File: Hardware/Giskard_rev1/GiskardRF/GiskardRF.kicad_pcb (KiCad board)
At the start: 4 copper layers, 79.8 x 43.7 mm, 68 parts, among them J101 USB_B_Micro, J102 Conn_ARM_JTAG_SWD_20, J103 Test pins COMM2, J104 Test pins COMM1, J201 SMA6252A23G50, J305 Conn_01x16, J306 Conn_01x16, SW101 RESET, U101 USBLC6-2P6, U102 FT230XQ, U103 AP22802AW5-7, U104 AP2127K-3.3, U105 M24C16-RM, U106 STM32G070CBTx, U107 APX823, U201 RFM69HW, U303 AP22802AW5-7, Y101 3225-16M-SR 16MHz 9pF, Y102 32.768K-CFPX217

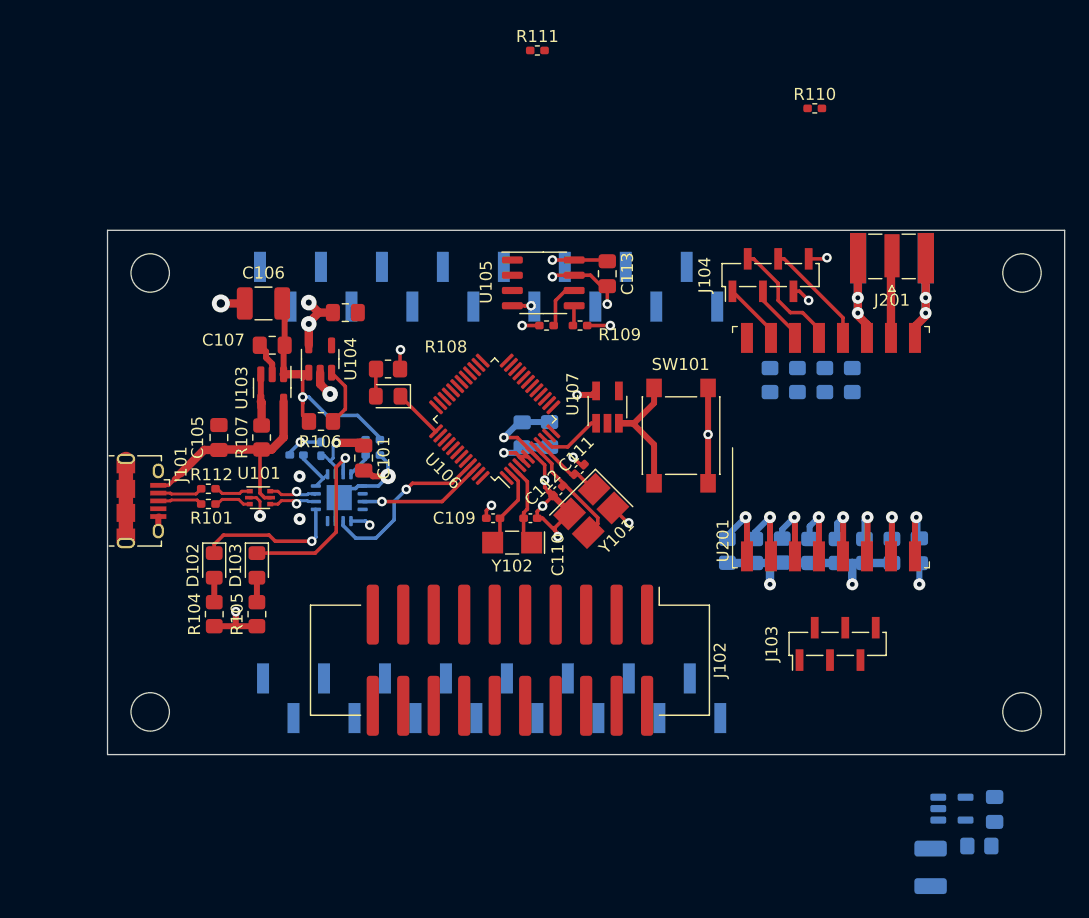
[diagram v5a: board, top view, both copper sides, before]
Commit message: Finished Giskard layout
- Need to fix DRC violations
- It'd be nice to move EEPROM closer to MPU
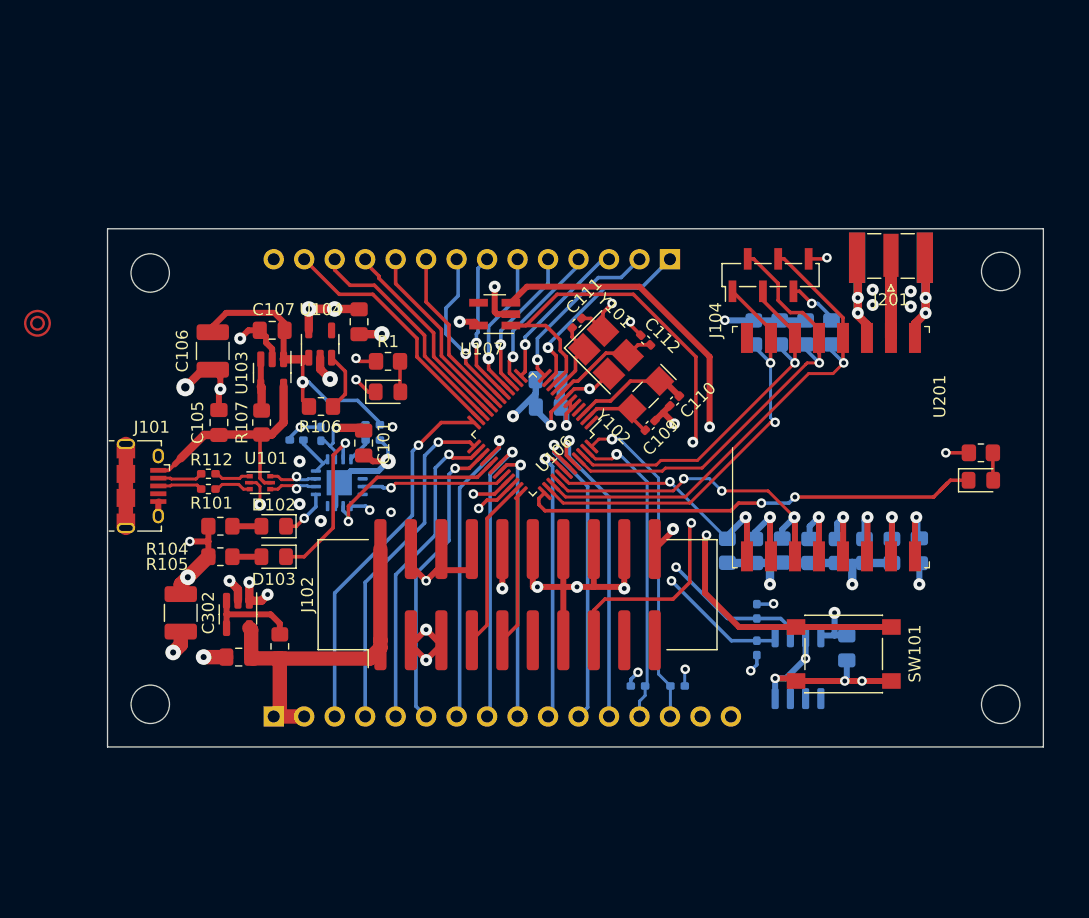
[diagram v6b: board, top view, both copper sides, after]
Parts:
- removed J103: Test pins COMM2, Connector_PinSocket_1.27mm:PinSocket_1x06_P1.27mm_Vertical_SMD_Pin1Left
- added D1: PWR_LED, Diode_SMD:D_0805_2012Metric_Pad1.15x1.40mm_HandSolder, F.Cu at (135.9, 109.5)
- added R1: 330, Resistor_SMD:R_0805_2012Metric_Pad1.20x1.40mm_HandSolder, F.Cu at (135.9, 106.9)
- C113, R108, R109, R110, R111, U105: moved to B.Cu
- C301, C302, R301, U303: moved to F.Cu
- J305: value Conn_01x16 -> Conn_01x14; footprint Connector_PinHeader_2.54mm:PinHeader_1x16_P2.54mm_Vertical_SMD_Pin1Left -> Connector_PinHeader_2.54mm:PinHeader_1x14_P2.54mm_Vertical
- J306: footprint Connector_PinHeader_2.54mm:PinHeader_1x16_P2.54mm_Vertical_SMD_Pin1Left -> Connector_PinHeader_2.54mm:PinHeader_1x16_P2.54mm_Vertical
- R102, R104, R105: value 270 -> 330
- moved C302 66.0 mm to (118.6, 127.9), turned to -90 degrees
- moved C301 64.3 mm to (123.4, 131.6), turned to 180 degrees
- moved U303 61.7 mm to (123.4, 128.0), turned to -90 degrees
- moved R301 60.6 mm to (126.9, 130.7), turned to 90 degrees
- moved R111 54.2 mm to (160.0, 134.0), turned to 180 degrees
- moved R110 50.3 mm to (156.7, 134.0)
- moved R102 49.9 mm to (185.3, 114.6), turned to 0 degrees
- moved D101 49.9 mm to (185.3, 116.8), turned to 0 degrees
- moved U105 38.5 mm to (170.1, 132.5), turned to 90 degrees
- moved C113 37.0 mm to (174.1, 130.8)
- moved R109 30.6 mm to (166.6, 130.8), turned to 90 degrees
- moved R108 29.6 mm to (166.6, 127.8), turned to -90 degrees
- moved SW101 22.7 mm to (173.9, 131.3), turned to 180 degrees
- moved J306 18.2 mm to (126.4, 136.5)
- moved Y102 16.6 mm to (157.4, 109.7), turned to -135 degrees
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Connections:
- J305 pad 1: GNDD -> /GPIO_PA0
- J305 pad 10: /GPIO_PA0 -> /GPIO_PB1
- J305 pad 11: /GPIO_PA8 -> /GPIO_PB2
- J305 pad 12: /GPIO_PB15 -> /GPIO_PB10
- J305 pad 13: /GPIO_PB14 -> /GPIO_PB11
- J305 pad 14: /GPIO_PB13 -> GNDD
- J305 pad 2: GNDD -> /GPIO_PA1
- J305 pad 3: /GPIO_PA3 -> /GPIO_PA2
- J305 pad 4: /GPIO_PA4 -> /GPIO_PA3
- J305 pad 5: /SPI1_SCK -> /GPIO_PA4
- J305 pad 6: /SPI1_MISO -> /SPI1_SCK
- J305 pad 7: /SPI1_MOSI -> /SPI1_MISO
- J305 pad 8: /GPIO_PA2 -> /SPI1_MOSI
- J305 pad 9: /GPIO_PA1 -> /GPIO_PB0
- J306 pad 11: /GPIO_PC13 -> /GPIO_PB4
- J306 pad 12: /GPIO_PB9 -> /GPIO_PB5
- J306 pad 13: /GPIO_PB8 -> /I2C1_SCL
- J306 pad 14: /GPIO_PB4 -> /I2C1_SDA
- J306 pad 2: /GPIO_PD0 -> /CON_PWR
- J306 pad 3: /GPIO_PD1 -> /GPIO_PB12
- J306 pad 4: /GPIO_PD2 -> /GPIO_PB13
- J306 pad 5: /GPIO_PC7 -> /GPIO_PB14
- J306 pad 6: /GPIO_PC6 -> /GPIO_PB15
- J306 pad 7: /I2C1_SCL -> /GPIO_PA8
- J306 pad 8: /I2C1_SDA -> /GPIO_PC6
- J306 pad 9: /GPIO_PD3 -> /GPIO_PC7
- U106 pad 19: /RF_RESET -> /GPIO_PB0
- U106 pad 20: /RF_FIFO_F_NE -> /GPIO_PB1
- U106 pad 21: /SPI2_MISO -> /GPIO_PB2
- U106 pad 22: /SPI2_SCK -> /GPIO_PB10
- U106 pad 23: /SPI2_MOSI -> /GPIO_PB11
- U106 pad 24: /SPI2_NSS -> /GPIO_PB12
- U106 pad 29: /I2C1_SCL -> /USART1_TX
- U106 pad 32: /I2C1_SDA -> /USART1_RX
- U106 pad 38: /GPIO_PD0 -> /SPI2_NSS
- U106 pad 39: /GPIO_PD1 -> /SPI2_SCK
- U106 pad 40: /GPIO_PD2 -> /RF_FIFO_F_NE
- U106 pad 41: /GPIO_PD3 -> /RF_RESET
- U106 pad 45: /USART1_TX -> /SPI2_MISO
- U106 pad 46: /USART1_RX -> /SPI2_MOSI
- U106 pad 47: /GPIO_PB8 -> /I2C1_SCL
- U106 pad 48: /GPIO_PB9 -> /I2C1_SDA
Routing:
- net GNDD: track 117.3 -> 190.3 mm, vias 27 -> 49
- net /~{RESET}: track 5.33 -> 58.6 mm, vias 0 -> 2
- net Net-(SW101-A): track 11.8 -> 56.1 mm, vias 0 -> 2
- net /~{ERR_LED}: track 4.29 -> 39.5 mm, vias 0 -> 2
- net /I2C2_SCL_MEM: track 1.70 -> 36.4 mm, vias 0 -> 2
- net /SPI2_SCK: track 9.12 -> 42.4 mm, vias 0 -> 1
- net /SPI2_NSS: track 5.22 -> 36.7 mm, vias 0 -> 2
- net /GPIO_PB12: track 0.00 -> 30.9 mm, vias 0 -> 1
- net /I2C2_SDA_MEM: track 4.05 -> 34.9 mm, vias 0 -> 2
- net /CON_PWR: track 0.00 -> 29.5 mm
- net /GPIO_PB13: track 0.00 -> 28.5 mm, vias 0 -> 1
- net /SPI2_MISO: track 9.93 -> 38.2 mm, vias 0 -> 1
- net /I2C1_SDA: track 0.00 -> 27.5 mm, vias 0 -> 1
- net /GPIO_PB5: track 0.00 -> 26.6 mm, vias 0 -> 1
- net /GPIO_PB4: track 0.00 -> 26.5 mm, vias 0 -> 1
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- added copper zone on In2.Cu, net +3V3
- added copper zone on In1.Cu, net GNDD
- added copper zone on In2.Cu, net GNDD
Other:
- board size 79.8 x 43.7 mm -> 78 x 43.2 mm

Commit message: Finished board layout
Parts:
- D101: value ERR_LED (RED) -> ERR_LED
- moved D1 49.4 mm to (185.2, 112.8)
- moved R1 49.4 mm to (185.2, 110.2)
- moved C113 22.7 mm to (152.0, 125.6)
- moved U105 22.7 mm to (148.0, 127.3)
- moved R109 22.3 mm to (145.8, 122.8), turned to 0 degrees
- moved R108 18.5 mm to (148.8, 122.8), turned to 180 degrees
- moved R102 2.80 mm to (185.2, 117.3)
- moved D101 2.79 mm to (185.3, 119.6)
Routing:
- net /I2C2_SCL_MEM: track 36.4 -> 12.0 mm, vias 2 -> 1
- net /I2C2_SDA_MEM: track 34.9 -> 11.2 mm, vias 2 -> 1
- net +3V3: track 62.1 -> 80.3 mm
- net /GPIO_PC7: track 23.1 -> 29.1 mm
- net /GPIO_PC6: track 24.8 -> 29.0 mm
- net /GPIO_PB3: track 24.1 -> 28.1 mm
- net /GPIO_PA8: track 26.4 -> 28.8 mm
- net /GPIO_PB4: track 26.5 -> 28.9 mm
- net /GPIO_PB5: track 26.6 -> 28.8 mm
- net /SPI2_NSS: track 36.7 -> 38.2 mm
- net GNDD: track 190.3 -> 191.8 mm, vias 49 -> 44
- net /~{ERR_LED}: track 39.5 -> 38.3 mm
- net /USART1_RX: track 12.2 -> 13.4 mm
- net /~{RESET}: track 58.6 -> 59.7 mm
- net /RF_RESET: track 21.8 -> 22.8 mm
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- added copper zone on F.Cu, net GNDD

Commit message: Final pcb adjustments
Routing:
- net GNDD: track 191.8 -> 194.1 mm, vias 44 -> 56
- added copper zone on B.Cu, net GNDD
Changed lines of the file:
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@@
   (via (at 120.523 131.572) (size 1.3) (drill 0.5) (layers "F.Cu" "B.Cu") (net 2))
   (via (at 167.72 125.51125) (size 1) (drill 0.4) (layers "F.Cu" "B.Cu") (net 2))
+  (via (at 176.53 135.636) (size 0.9) (drill 0.4) (layers "F.Cu" "B.Cu") (net 2))
   (via (at 136.652 112.268) (size 0.9) (drill 0.4) (layers "F.Cu" "B.Cu") (free) (net 2))
   (via (at 135.636 116.586) (size 0.9) (drill 0.4) (layers "F.Cu" "B.Cu") (free) (net 2))
@@
   (via (at 146.304 111.506) (size 1) (drill 0.4) (layers "F.Cu" "B.Cu") (net 2))
   (via (at 171.45 101.854) (size 0.9) (drill 0.4) (layers "F.Cu" "B.Cu") (net 2))
+  (via (at 176.53 131.572) (size 0.9) (drill 0.4) (layers "F.Cu" "B.Cu") (net 2))
   (via (at 156.083 103.632) (size 0.9) (drill 0.4) (layers "F.Cu" "B.Cu") (net 2))
   (via (at 176.276 100.965) (size 1) (drill 0.4) (layers "F.Cu" "B.Cu") (net 2))
   (via (at 130.294002 120.234206) (size 1) (drill 0.4) (layers "F.Cu" "B.Cu") (free) (net 2))
+  (via (at 171.958 135.636) (size 0.9) (drill 0.4) (layers "F.Cu" "B.Cu") (net 2))
   (via (at 144.78 100.711) (size 1) (drill 0.4) (layers "F.Cu" "B.Cu") (net 2))
+  (via (at 167.386 135.636) (size 0.9) (drill 0.4) (layers "F.Cu" "B.Cu") (net 2))
   (via (at 152.68136 109.22) (size 0.9) (drill 0.4) (layers "F.Cu" "B.Cu") (net 2))
   (via (at 139.065 131.826) (size 1) (drill 0.4) (layers "F.Cu" "B.Cu") (net 2))
+  (via (at 171.958 127.254) (size 0.9) (drill 0.4) (layers "F.Cu" "B.Cu") (net 2))
   (via (at 139.065 129.286) (size 1) (drill 0.4) (layers "F.Cu" "B.Cu") (net 2))
+  (via (at 172.72 112.014) (size 0.9) (drill 0.4) (layers "F.Cu" "B.Cu") (net 2))
+  (via (at 177.292 112.014) (size 0.9) (drill 0.4) (layers "F.Cu" "B.Cu") (net 2))
   (via (at 172.466 98.298) (size 0.9) (drill 0.4) (layers "F.Cu" "B.Cu") (net 2))
   (via (at 180.689 101.63525) (size 1) (drill 0.4) (layers "F.Cu" "B.Cu") (net 2))
@@
   (via (at 128.27 115.201052) (size 1) (drill 0.4) (layers "F.Cu" "B.Cu") (free) (net 2))
   (via (at 180.166 125.51125) (size 1) (drill 0.4) (layers "F.Cu" "B.Cu") (net 2))
+  (via (at 177.292 115.57) (size 0.9) (drill 0.4) (layers "F.Cu" "B.Cu") (net 2))
+  (via (at 172.72 115.57) (size 0.9) (drill 0.4) (layers "F.Cu" "B.Cu") (net 2))
   (via (at 128.27 118.8974) (size 1) (drill 0.4) (layers "F.Cu" "B.Cu") (free) (net 2))
   (via (at 179.451 102.362) (size 1) (drill 0.4) (layers "F.Cu" "B.Cu") (net 2))
@@
   (via (at 179.451 101.092) (size 1) (drill 0.4) (layers "F.Cu" "B.Cu") (net 2))
   (via (at 118.999 109.093) (size 1.5) (drill 0.7) (layers "F.Cu" "B.Cu") (net 2))
+  (via (at 171.958 131.572) (size 0.9) (drill 0.4) (layers "F.Cu" "B.Cu") (net 2))
   (via (at 135.89 114.554) (size 1.3) (drill 0.5) (layers "F.Cu" "B.Cu") (net 2))
   (via (at 148.082 112.268) (size 0.9) (drill 0.4) (layers "F.Cu" "B.Cu") (net 2))
   (via (at 175.039 102.90525) (size 1) (drill 0.4) (layers "F.Cu" "B.Cu") (net 2))
   (via (at 128.537226 112.321445) (size 0.9) (drill 0.4) (layers "F.Cu" "B.Cu") (net 2))
+  (via (at 167.386 131.572) (size 0.9) (drill 0.4) (layers "F.Cu" "B.Cu") (net 2))
   (via (at 159.766 112.141) (size 0.9) (drill 0.4) (layers "F.Cu" "B.Cu") (net 2))
   (via (at 117.983 131.191) (size 1.3) (drill 0.5) (layers "F.Cu" "B.Cu") (net 2))
   (via (at 174.578 125.51125) (size 1) (drill 0.4) (layers "F.Cu" "B.Cu") (net 2))
+  (via (at 177.292 108.458) (size 0.9) (drill 0.4) (layers "F.Cu" "B.Cu") (net 2))
   (via (at 145.288 126.492) (size 0.9) (drill 0.4) (layers "F.Cu" "B.Cu") (net 2))
   (via (at 149.098 126.6405) (size 1.3) (drill 0.5) (layers "F.Cu" "B.Cu") (net 2))
@@
   (segment (start 132.801 116.069) (end 131.826 117.044) (width 0.5) (layer "B.Cu") (net 2))
   (segment (start 135.89 114.554) (end 135.89 114.1605) (width 0.3) (layer "B.Cu") (net 2))
+  (segment (start 131.501 119.862231) (end 131.129025 120.234206) (width 0.5) (layer "B.Cu") (net 2))
   (segment (start 131.501 117.369) (end 131.826 117.044) (width 0.3) (layer "B.Cu") (net 2))
   (segment (start 148.082 112.268) (end 148.209 112.141) (width 0.5) (layer "B.Cu") (net 2))
   (segment (start 148.4415 126.6405) (end 146.05 129.032) (width 0.5) (layer "B.Cu") (net 2))
   (segment (start 148.209 112.141) (end 148.209 110.744) (width 0.5) (layer "B.Cu") (net 2))
+  (segment (start 131.501 118.994) (end 131.501 119.862231) (width 0.5) (layer "B.Cu") (net 2))
   (segment (start 135.89 114.1605) (end 135.2175 113.488) (width 0.3) (layer "B.Cu") (net 2))
   (segment (start 148.209 109.601) (end 148.209 108.4795) (width 0.5) (layer "B.Cu") (net 2))
@@
   (segment (start 148.59 126.1325) (end 148.59 124.679) (width 0.5) (layer "B.Cu") (net 2))
   (segment (start 128.537226 112.321445) (end 127.7025 113.156171) (width 0.3) (layer "B.Cu") (net 2))
+  (segment (start 131.129025 120.234206) (end 130.294002 120.234206) (width 0.5) (layer "B.Cu") (net 2))
   (segment (start 128.537226 112.321445) (end 128.628281 112.4125) (width 0.3) (layer "B.Cu") (net 2))
   (segment (start 131.501 118.994) (end 131.501 117.369) (width 0.5) (layer "B.Cu") (net 2))
@@
   (segment (start 140.97 106.398554) (end 140.97 103.886) (width 0.3) (layer "F.Cu") (net 87))
   (zone (net 2) (net_name "GNDD") (layer "F.Cu") (hatch edge 0.5)
+    (priority 4)
+    (connect_pads (clearance 0.4))
+    (min_thickness 0.3) (filled_areas_thickness no)
+    (fill yes (thermal_gap 0.5) (thermal_bridge_width 0.5))
+    (polygon
+      (pts
+        (xy 182.88 101.6)
+        (xy 185.42 103.632)
+        (xy 189.23 103.632)
+        (xy 189.23 131.826)
+        (xy 184.404 131.826)
+        (xy 182.88 134.366)
+        (xy 182.88 138.43)
+        (xy 120.65 138.43)
+        (xy 120.65 135.128)
+        (xy 117.856 131.826)
+        (xy 113.538 131.826)
+        (xy 113.538 103.378)
+        (xy 118.11 103.378)
+        (xy 119.888 101.092)
+        (xy 119.888 96.52)
+        (xy 182.88 96.52)
+      )
+    )
+    (polygon
+      (pts
+        (xy 142.748 101.346)
+        (xy 142.748 104.902)
+        (xy 147.066 104.902)
+        (xy 147.066 101.346)
+        (xy 142.748 101.346)
+        (xy 142.748 101.346)
+      )
+    )
+  )
+  (zone (net 2) (net_name "GNDD") (layer "F.Cu") (hatch edge 0.5)
     (priority 3)
     (connect_pads (clearance 0.4))
@@
       (pts
         (xy 182.88 101.6)
-        (xy 185.42 103.505)
-        (xy 189.23 103.505)
+        (xy 185.42 103.632)
+        (xy 189.23 103.632)
         (xy 189.23 131.826)
-        (xy 184.531 131.826)
-        (xy 183.007 134.493)
-        (xy 183.007 138.303)
-        (xy 120.65 138.303)
-        (xy 120.65 135.255)
-        (xy 118.11 132.08)
-        (xy 113.665 132.08)
-        (xy 113.665 103.505)
-        (xy 118.11 103.505)
-        (xy 120.015 100.965)
-        (xy 120.015 96.52)
+        (xy 184.404 131.826)
+        (xy 182.88 134.366)
+        (xy 182.88 138.43)
+        (xy 120.65 138.43)
+        (xy 120.65 135.128)
+        (xy 117.856 131.826)
+        (xy 113.538 131.826)
+        (xy 113.665 103.378)
+        (xy 118.11 103.378)
+        (xy 119.888 101.092)
+        (xy 119.888 96.52)
         (xy 175.26 96.52)
         (xy 180.34 96.52)
@@
     (polygon
       (pts
+        (xy 173.482 96.52)
+        (xy 173.482 101.6)
+        (xy 174.498 103.886)
+        (xy 174.498 107.188)
+        (xy 181.356 107.188)
+        (xy 181.356 104.14)
         (xy 182.88 101.6)
-        (xy 185.42 103.505)
-        (xy 189.23 103.505)
+        (xy 185.42 103.632)
+        (xy 189.23 103.632)
         (xy 189.23 131.826)
-        (xy 184.531 131.826)
-        (xy 183.007 134.493)
-        (xy 183.007 138.303)
-        (xy 120.65 138.303)
-        (xy 120.65 135.255)
-        (xy 118.11 132.08)
-        (xy 113.665 132.08)
-        (xy 113.665 103.505)
-        (xy 118.11 103.505)
-        (xy 120.015 100.965)
-        (xy 120.015 96.52)
-        (xy 182.88 96.52)
+        (xy 184.404 131.826)
+        (xy 182.88 134.366)
+        (xy 182.88 138.43)
+        (xy 120.65 138.43)
+        (xy 120.65 135.128)
+        (xy 117.856 131.826)
+        (xy 113.538 131.826)
+        (xy 113.665 103.378)
+        (xy 118.11 103.378)
+        (xy 119.888 100.965)
+        (xy 119.888 96.52)
       )
     )
     (polygon
       (pts
-        (xy 119.888 115.9256)
         (xy 119.888 117.983)
         (xy 121.92 117.983)
         (xy 121.92 115.9256)
+        (xy 119.888 115.9256)
       )
     )
+  )
+  (zone (net 2) (net_name "GNDD") (layer "B.Cu") (hatch edge 0.5)
+    (priority 5)
+    (connect_pads (clearance 0.4))
+    (min_thickness 0.3) (filled_areas_thickness no)
+    (fill yes (thermal_gap 0.5) (thermal_bridge_width 0.4))
+    (polygon
+      (pts
+        (xy 189.23 103.632)
+        (xy 189.23 131.826)
+        (xy 184.404 131.826)
+        (xy 182.88 134.366)
+        (xy 182.88 138.43)
+        (xy 120.65 138.43)
+        (xy 120.65 135.128)
+        (xy 117.856 131.826)
+        (xy 113.538 131.826)
+        (xy 113.665 103.378)
+        (xy 118.11 103.378)
+        (xy 119.888 100.965)
+        (xy 119.888 96.52)
+        (xy 173.482 96.52)
+        (xy 173.482 101.6)
+        (xy 174.498 103.886)
+        (xy 174.498 107.188)
+        (xy 181.356 107.188)
+        (xy 181.356 104.14)
+        (xy 182.88 101.6)
+        (xy 185.42 103.632)
+      )
+    )
